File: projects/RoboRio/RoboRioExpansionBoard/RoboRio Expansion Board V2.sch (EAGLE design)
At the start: 80 parts, among them J1 RRINTERFACE-FEMALE, J2 MICROSD, Q1 5.0 MHz, T1 NPN-SOT416, U1 P8X32A-Q44, U2 24LC256ST, U3 FT232RFTR232R, U4 MC1525TO

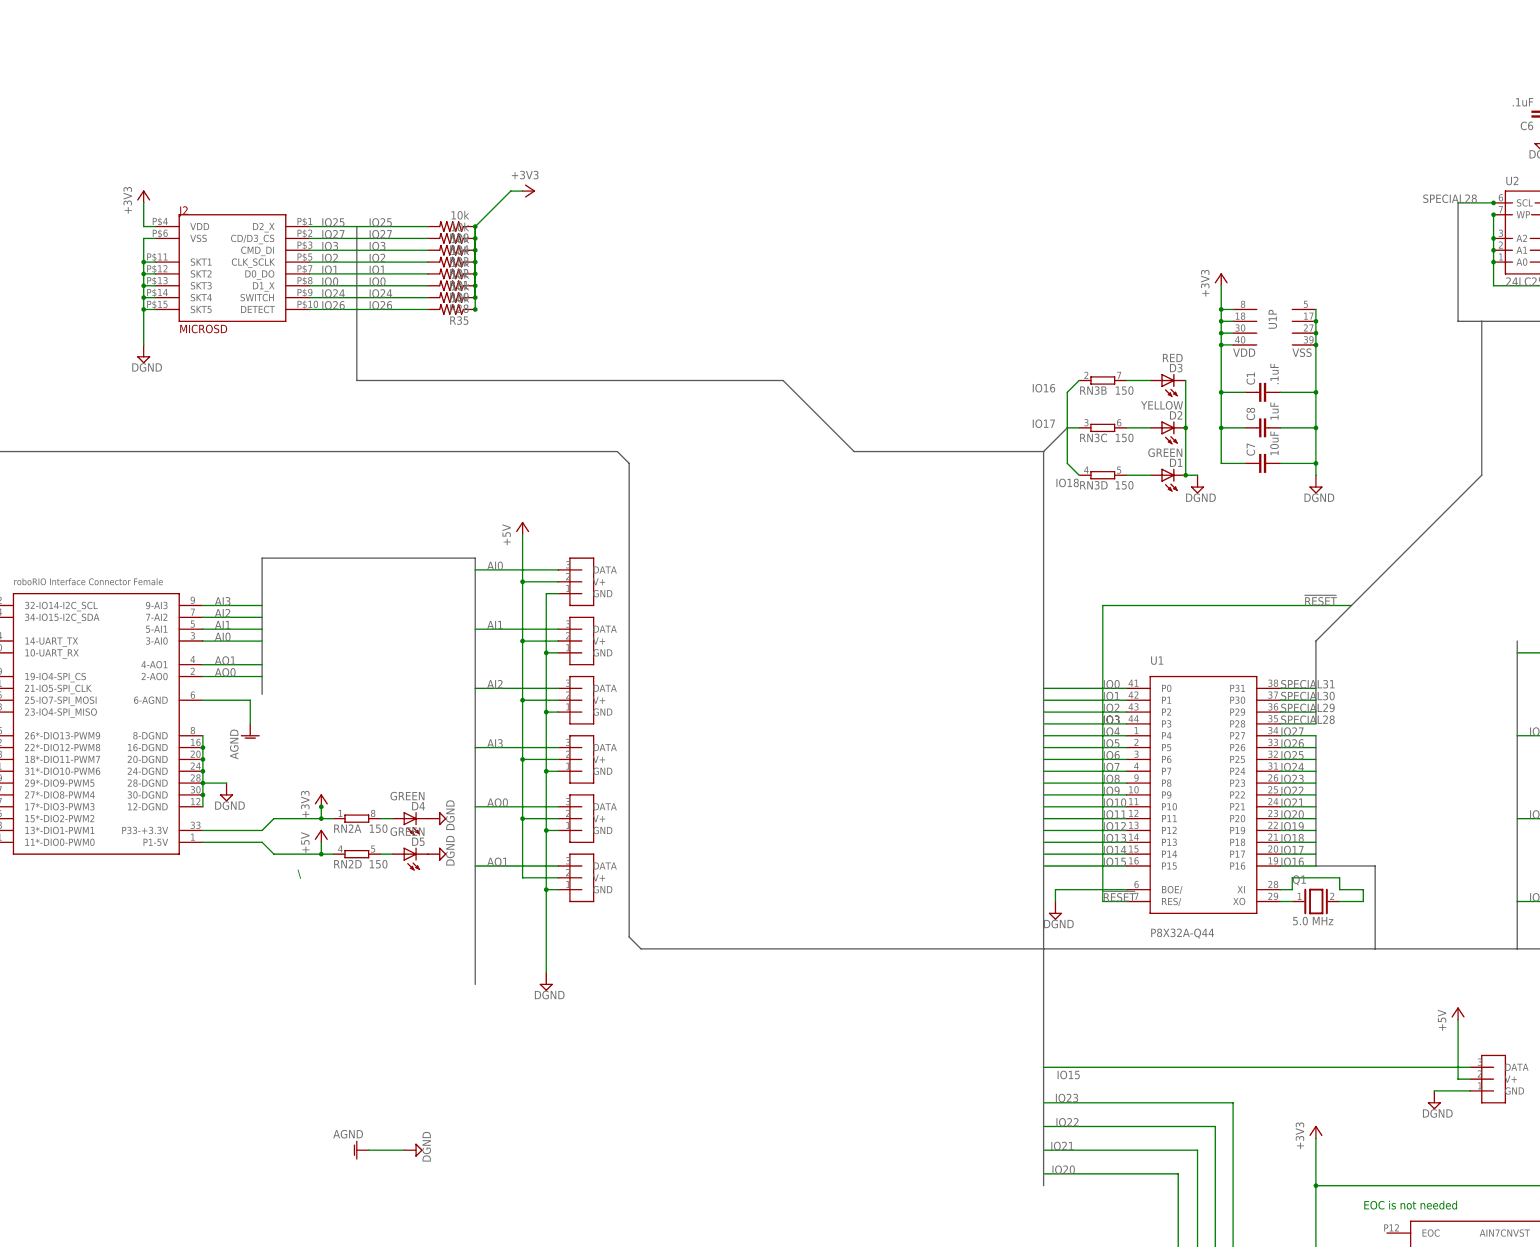
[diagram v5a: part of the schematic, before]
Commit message: Preparing for our new power supply design
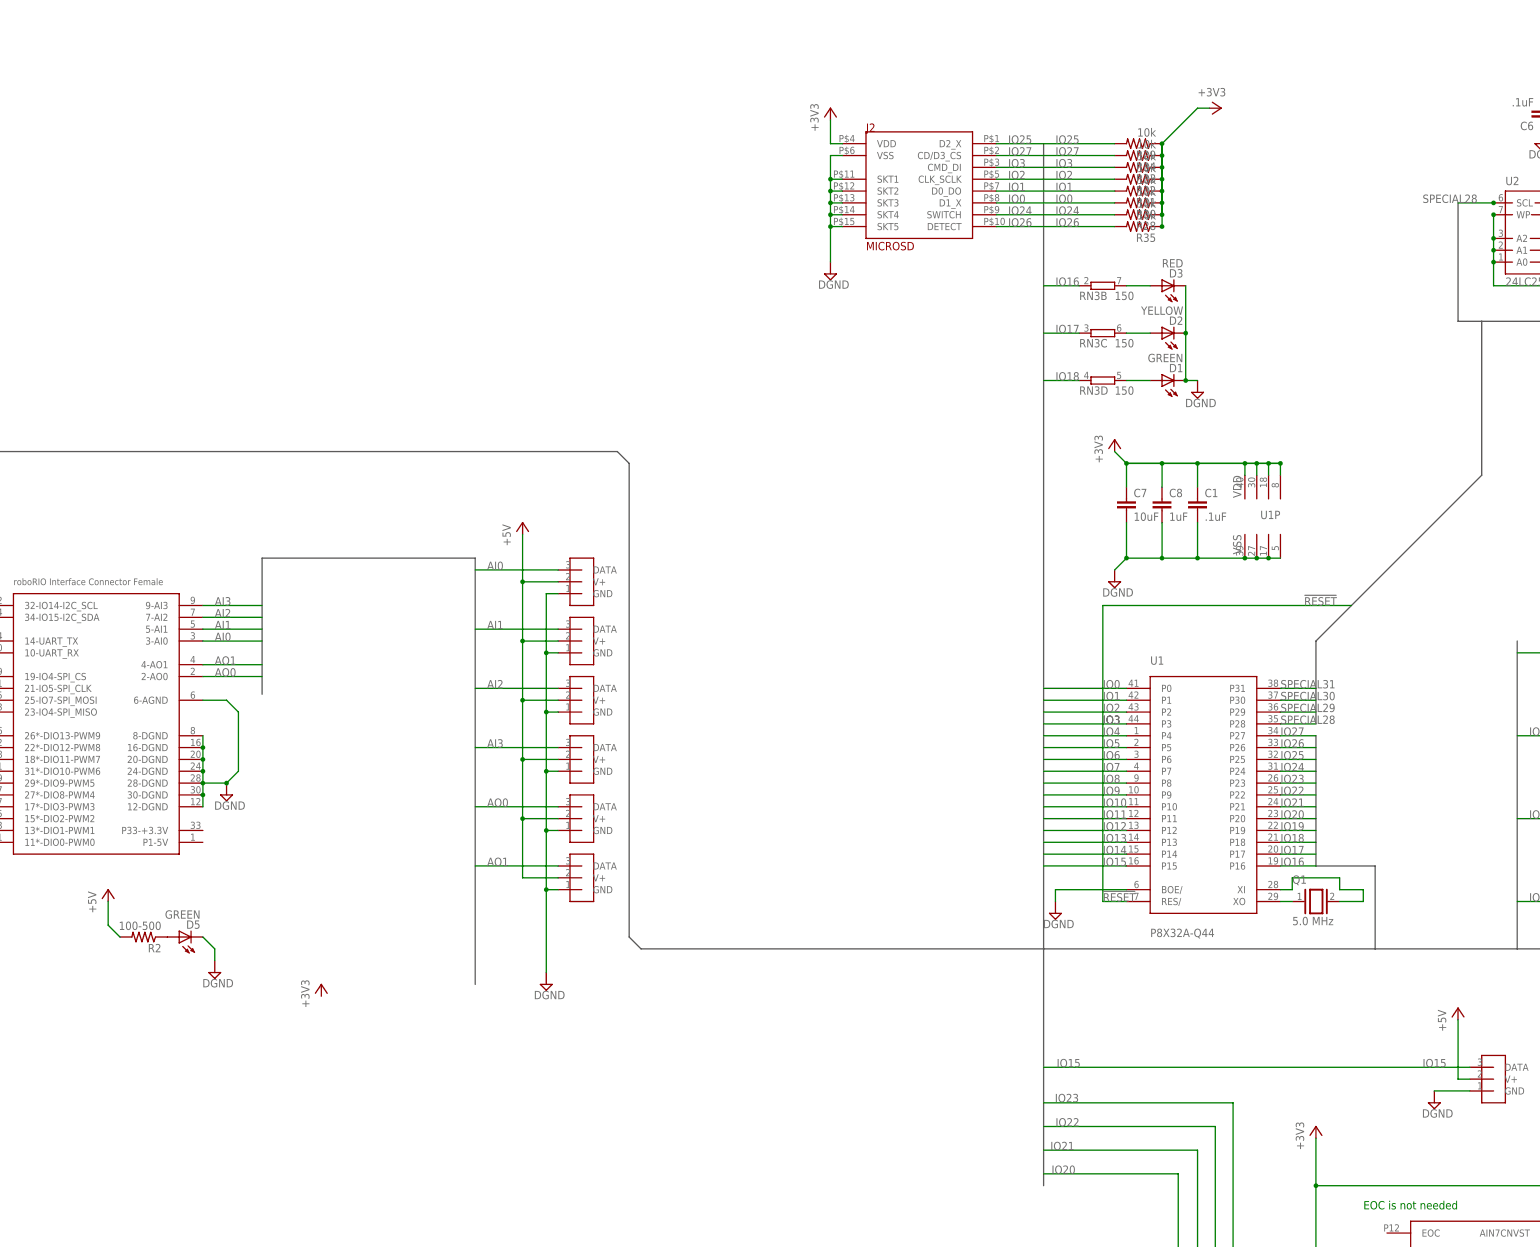
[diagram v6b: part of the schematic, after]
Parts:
- removed D4: GREEN, led:LEDCHIPLED_0603
- removed RN2: 150, resistor-dil:4R-N0402ARV341
- added R2: 100-500, resistor:R-US_R0603
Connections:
- removed net AGND: J1.6-AGND
- removed net L1: D4.A, RN2A.2
- net +3V3: no longer J1.P33-+3.3V, RN2A.1
- net +5V: now also R2.2, U$17.V+; no longer J1.P1-5V, RN2D.1
- net DGND: now also J1.6-AGND; no longer D4.C
- net N$16: now also U$17.DATA
- net N$4: now also R2.1; no longer RN2D.2
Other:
- note removed: "\"
- moved on the sheet: C1, C7, C8, D1, D2, D3, D5, J2, R28, R29, R30, R31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

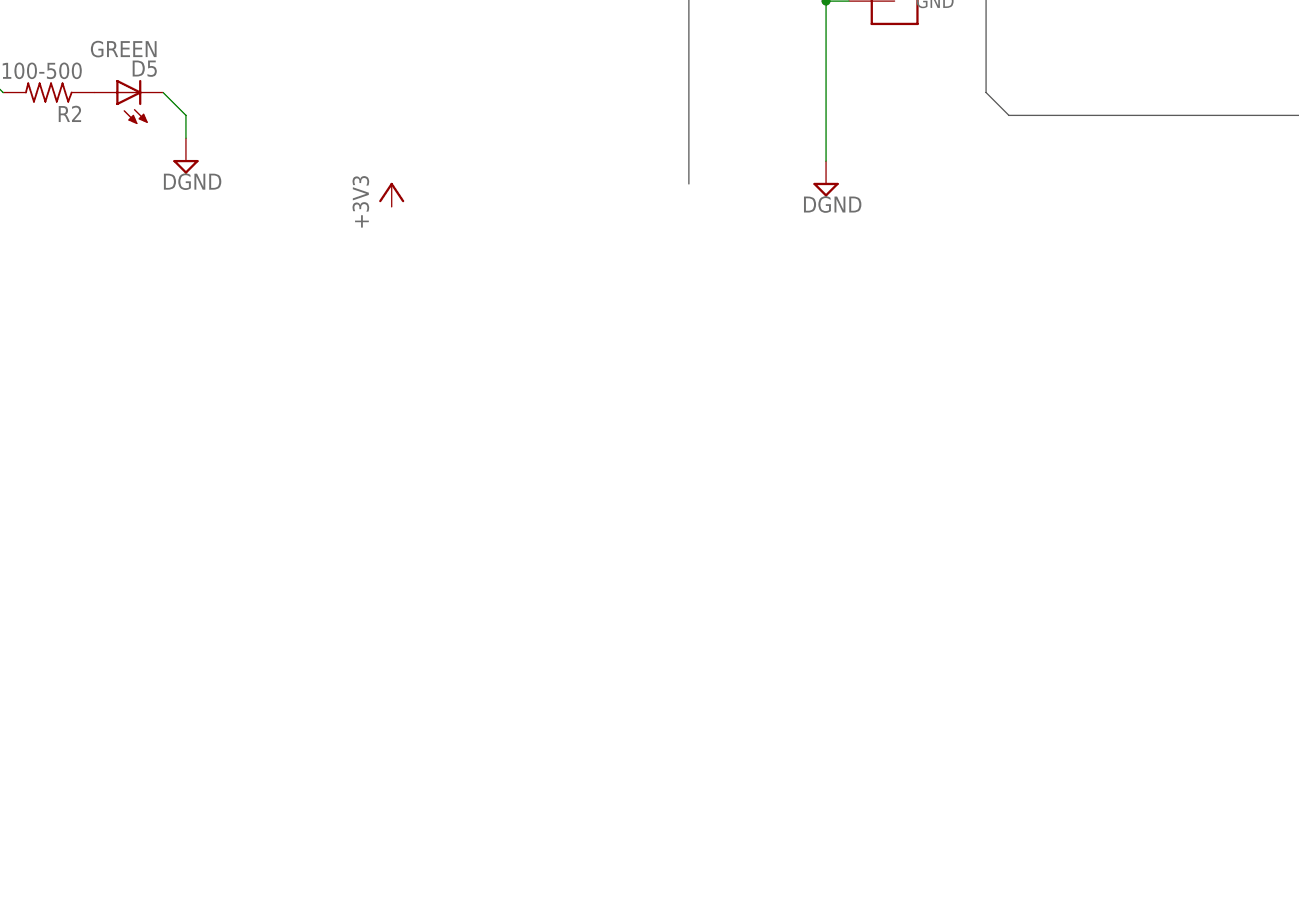
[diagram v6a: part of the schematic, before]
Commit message: Added a single 3.3v regulator
We probably won't use this one, but it is very easy to remove
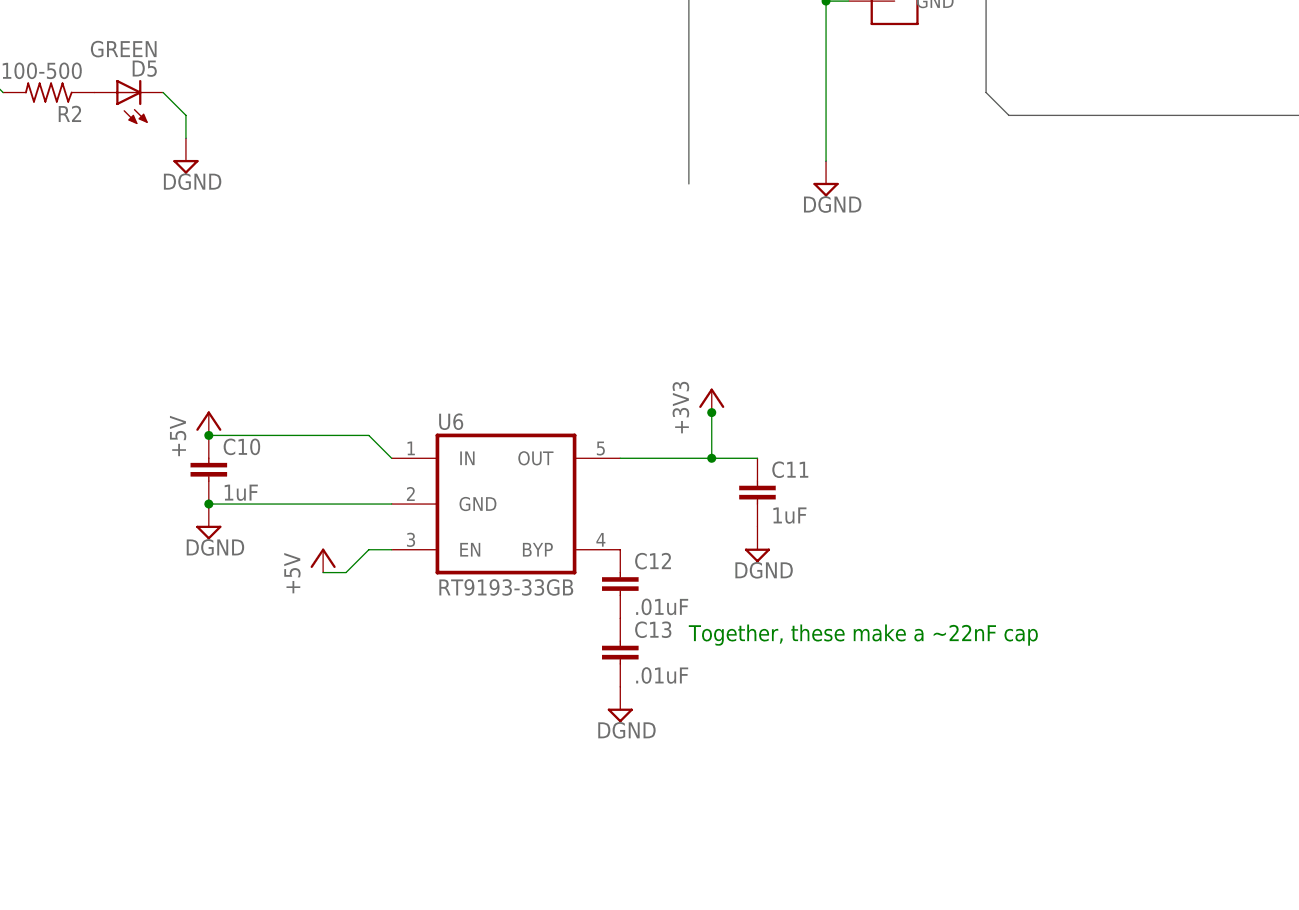
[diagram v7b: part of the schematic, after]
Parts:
- added C10, C11: 1uF, resistor:C-EUC0603K
- added C12, C13: .01uF, resistor:C-EUC0603K
- added U6: RT9193-33GB, dp_devices:VREG_5PINS-SOT-23-5
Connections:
- new net N$11: C12.2, C13.1
- new net N$22: C12.1, U6.BYP
- net +3V3: now also C11.1, U6.OUT
- net +5V: now also C10.1, U6.EN, U6.IN
- net DGND: now also C10.2, C11.2, C13.2, U6.GND
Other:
- note added: "Together, these make a ~22nF cap"
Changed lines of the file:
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@@
 <part name="U$37" library="3pin" deviceset="3PINDEVICE" device="DEFAULT"/>
 <part name="R2" library="resistor" deviceset="R-US_" device="R0603" value="100-500"/>
+<part name="U6" library="dp_devices" deviceset="VREG_5PINS" device="-SOT-23-5" value="RT9193-33GB"/>
+<part name="C10" library="resistor" deviceset="C-EU" device="C0603K" value="1uF"/>
+<part name="P+10" library="supply1" deviceset="+5V" device=""/>
+<part name="C11" library="resistor" deviceset="C-EU" device="C0603K" value="1uF"/>
+<part name="C12" library="resistor" deviceset="C-EU" device="C0603K" value=".01uF"/>
+<part name="C13" library="resistor" deviceset="C-EU" device="C0603K" value=".01uF"/>
+<part name="SUPPLY29" library="supply2" deviceset="DGND" device=""/>
+<part name="SUPPLY31" library="supply2" deviceset="DGND" device=""/>
+<part name="P+12" library="supply1" deviceset="+5V" device=""/>
+<part name="SUPPLY32" library="supply2" deviceset="DGND" device=""/>
 </parts>
 <sheets>
@@
 <plain>
 <text x="68.58" y="-55.88" size="1.778" layer="91">EOC is not needed</text>
+<text x="-121.92" y="-58.42" size="1.778" layer="91">Together, these make a ~22nF cap</text>
 </plain>
 <instances>
@@
 <instance part="D5" gate="G$1" x="-185.42" y="2.54" rot="R90"/>
 <instance part="SUPPLY39" gate="G$1" x="-177.8" y="-5.08"/>
-<instance part="+3V7" gate="G$1" x="-154.94" y="-7.62"/>
+<instance part="+3V7" gate="G$1" x="-119.38" y="-30.48"/>
 <instance part="P+16" gate="1" x="-200.66" y="12.7"/>
 <instance part="+3V3" gate="G$1" x="116.84" y="60.96" rot="R90"/>
@@
 <instance part="U$37" gate="G$1" x="96.52" y="-27.94" rot="R180"/>
 <instance part="R2" gate="G$1" x="-193.04" y="2.54" rot="R180"/>
+<instance part="U6" gate="G$1" x="-142.24" y="-43.18"/>
+<instance part="C10" gate="G$1" x="-175.26" y="-38.1"/>
+<instance part="P+10" gate="1" x="-175.26" y="-33.02"/>
+<instance part="C11" gate="G$1" x="-114.3" y="-40.64"/>
+<instance part="C12" gate="G$1" x="-129.54" y="-50.8"/>
+<instance part="C13" gate="G$1" x="-129.54" y="-58.42"/>
+<instance part="SUPPLY29" gate="G$1" x="-114.3" y="-48.26"/>
+<instance part="SUPPLY31" gate="G$1" x="-175.26" y="-45.72"/>
+<instance part="P+12" gate="1" x="-162.56" y="-48.26"/>
+<instance part="SUPPLY32" gate="G$1" x="-129.54" y="-66.04"/>
 </instances>
 <busses>
@@
 <pinref part="+3V7" gate="G$1" pin="+3V3"/>
 <pinref part="+3V7" gate="G$1" pin="+3V3"/>
+<pinref part="U6" gate="G$1" pin="OUT"/>
+<pinref part="C11" gate="G$1" pin="1"/>
+<wire x1="-114.3" y1="-38.1" x2="-119.38" y2="-38.1" width="0.1524" layer="91"/>
+<wire x1="-119.38" y1="-38.1" x2="-129.54" y2="-38.1" width="0.1524" layer="91"/>
+<wire x1="-119.38" y1="-38.1" x2="-119.38" y2="-33.02" width="0.1524" layer="91"/>
+<junction x="-119.38" y="-38.1"/>
+<junction x="-119.38" y="-33.02"/>
 </segment>
 <segment>
@@
 <pinref part="R2" gate="G$1" pin="2"/>
 </segment>
+<segment>
+<pinref part="U6" gate="G$1" pin="EN"/>
+<wire x1="-154.94" y1="-48.26" x2="-157.48" y2="-48.26" width="0.1524" layer="91"/>
+<wire x1="-157.48" y1="-48.26" x2="-160.02" y2="-50.8" width="0.1524" layer="91"/>
+<wire x1="-160.02" y1="-50.8" x2="-162.56" y2="-50.8" width="0.1524" layer="91"/>
+<pinref part="P+12" gate="1" pin="+5V"/>
+</segment>
+<segment>
+<pinref part="C10" gate="G$1" pin="1"/>
+<pinref part="P+10" gate="1" pin="+5V"/>
+<pinref part="U6" gate="G$1" pin="IN"/>
+<wire x1="-154.94" y1="-38.1" x2="-157.48" y2="-35.56" width="0.1524" layer="91"/>
+<wire x1="-157.48" y1="-35.56" x2="-175.26" y2="-35.56" width="0.1524" layer="91"/>
+<junction x="-175.26" y="-35.56"/>
+</segment>
 </net>
 <net name="AI3" class="0">
@@
 <pinref part="U$36" gate="G$1" pin="GND"/>
 </segment>
+<segment>
+<pinref part="C11" gate="G$1" pin="2"/>
+<pinref part="SUPPLY29" gate="G$1" pin="DGND"/>
+</segment>
+<segment>
+<pinref part="C10" gate="G$1" pin="2"/>
+<pinref part="SUPPLY31" gate="G$1" pin="DGND"/>
+<pinref part="U6" gate="G$1" pin="GND"/>
+<wire x1="-175.26" y1="-43.18" x2="-154.94" y2="-43.18" width="0.1524" layer="91"/>
+<junction x="-175.26" y="-43.18"/>
+</segment>
+<segment>
+<pinref part="C13" gate="G$1" pin="2"/>
+<pinref part="SUPPLY32" gate="G$1" pin="DGND"/>
+</segment>
 </net>
 <net name="N$8" class="0">
@@
 </segment>
 </net>
+<net name="N$11" class="0">
+<segment>
+<pinref part="C12" gate="G$1" pin="2"/>
+<pinref part="C13" gate="G$1" pin="1"/>
+</segment>
+</net>
+<net name="N$22" class="0">
+<segment>
+<pinref part="U6" gate="G$1" pin="BYP"/>
+<pinref part="C12" gate="G$1" pin="1"/>
+</segment>
+</net>
